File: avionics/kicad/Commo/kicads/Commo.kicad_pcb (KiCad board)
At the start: 4 copper layers, 55 x 35 mm, 81 parts, among them U1 ByA 100nF +3V3 U1-VDDA Bypass, U1 ByB 100nF +3V3 U1-VDD Bypass

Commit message: Migrate fleet TPM from Infineon SLB9670 to SLB9672
Replaces every active reference to the SLB9670 TPM with SLB9672 across
KiCad symbols/schematics/PCBs/netlists, generator scripts, firmware
device-tree overlays, and documentation (REFERENCES.md, WBS/TODO,
current-specification, graphical build guide). Archived files, frozen
revision snapshots, and the old datasheet PDF are left untouched.

- Added avionics/datasheets/SLB_9672XU20_Infineon.pdf (Infineon DS Rev
  1.3, 2024-11-18) and a new clean-room symbol/pinmap
  (Observer_SLB9672_TPM.kicad_sym, SLB9672XU2_0_pinmap.csv), replacing
  the superseded SLB9670 symbol/pinmap.
- Verified the physical footprint is unchanged (5x5mm body, 0.5mm
  pitch, 32-pin QFN, 3.6x3.6mm exposed pad per both datasheets), so the
  existing Package_DFN_QFN:QFN-32-1EP_5x5mm_P0.5mm_EP3.45x3.45mm
  footprint was reused as-is. Pin *functions* do differ (SLB9672 makes
  pins 1/14/22 the mandatory VDD pins vs 8/22 on SLB9670; pin 6 is now a
  true no-connect instead of GPIO; pins 3/4/7 are GPIO_00/01/02 instead
  of NCI/NCI/PP) -- the new symbol and every net-map/pinmap that lists
  pin functions reflect the corrected pinout.
- Populated the corrected component into Observer, Commo, Flight
  Engineer, and CAN-PERIPH-GW-1's schematics (lib_symbol block +
  instances) and into every board's PCB Value/property text. Pilot's
  and XO's own independently-authored inline TPM symbols were text-
  renamed only, preserving their pre-existing (and separately tracked)
  wrong-pin-number defect -- out of scope for this swap.
- Firmware: infineon,slb9670 -> infineon,slb9672 compatible string and
  tpm_slb9670: -> tpm_slb9672: node label in both active cape DTS
  overlays.
- REFERENCES.md REF-SENSOR-011 updated in place with validated Infineon
  URLs; new open items logged for (a) re-running kicad-cli ERC/DRC
  (unavailable in this environment) and (b) a newly-found, unrelated
  pre-existing footprint-mismatch defect on XO's placed TPM.
- PROJECT_INDEX.md / t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
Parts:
- TPM: value SLB9670 -> SLB9672
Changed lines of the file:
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@@
 			)
 		)
-		(property "Value" "SLB9670"
+		(property "Value" "SLB9672"
 			(at 0 -3.83 0)
 			(layer "B.Fab")

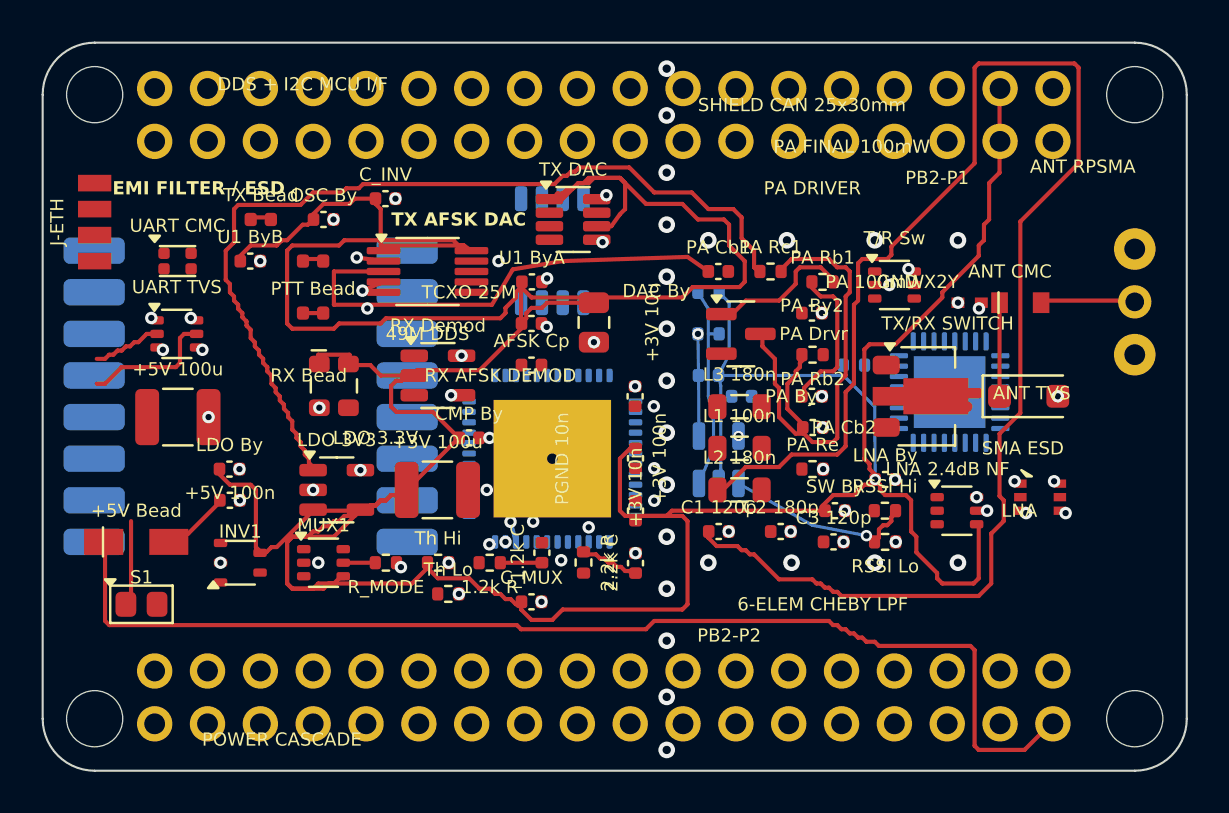
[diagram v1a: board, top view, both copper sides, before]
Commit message: feat(avionics): swap Commo's LoRa (RFM95W) for SiK (RFD900ux-SMT), ERC 0
Completes the other half of the XO<->Commo radio relocation: Commo
gains the SiK link SiK-side via a new one-off script
(swap_lora_for_sik.py) that does direct S-expression surgery rather
than re-running gen_commo_sch.py, which is PCB-first and already
confirmed drifted from the real board. Also fixes two pre-existing
circuit bugs the swap's ERC cleanup exposed: the T/R switch's antenna
pin was on a differently-named net one row away from the working ANT
filter chain (merged); and the PA final transistor's emitter pin was
wired straight to GND, bypassing its own degeneration resistor
(rewired onto PA_EMIT). DDS_FSYNC (the TX DAC's SPI chip-select,
previously unrouted) now uses the exact PB2 pin the LoRa->SiK swap
freed (ex-SPI1_CS_LORA), by explicit owner decision. kicad-cli sch
erc: 0 violations (down from 45).

PCB synced to match (schematic driving PCB, not the reverse): old
RFM95W footprint removed, 8 new SIK-chain footprints added with nets
matched 1:1 against the real schematic pin table. Along the way DRC
caught a real geometry bug in the shared RFDesign_RFD900ux_SMT
footprint (pad pitch/axis swap causing adjacent castellated pins to
short) -- fixed against RFD900ux DataSheet v1.2.pdf Table 6-1 and
confirmed via DRC. Residual: Commo's existing hand-placed layout has
no contiguous free region for the 21x29mm SIK module without touching
ETH-PHY/T-ETH -- flagged in WBS.md as needing a real floorplan pass,
not silently left implicit.

Co-Authored-By: Claude Sonnet 5 <noreply@anthropic.com>
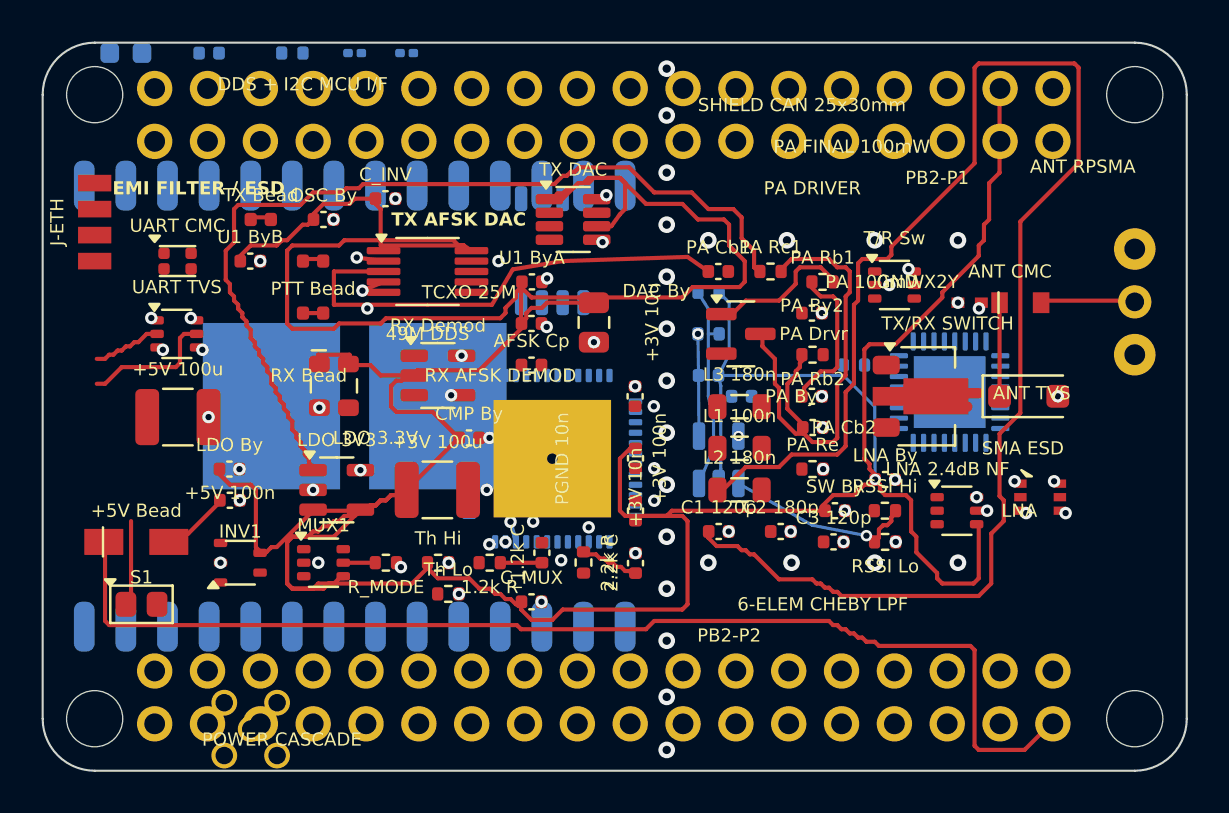
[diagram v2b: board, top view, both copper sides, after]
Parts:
- removed LoRa: RFM95W, HOPERF_RFM9XW_SMD
- added C-SIK-SH1: DNP, C_0201_0603Metric, B.Cu at (115.0, 100.5)
- added C-SIK-SH2: DNP, C_0201_0603Metric, B.Cu at (117.5, 100.5)
- added C-SIK1: 10uF 10V X5R, C_0603_1608Metric, B.Cu at (104.0, 100.5)
- added C-SIK2: 100nF, C_0402_1005Metric, B.Cu at (108.0, 100.5)
- added D-ANT-SIK: RCLAMP0502B, RCLAMP0502B_SOD882, B.Cu at (104.0, 133.0)
- added J-ANT-SIK: MMCX vertical, MMCX_Molex_73415-1471_Vertical, B.Cu at (110.0, 133.0)
- added L-SIK-SER: 0R link, R_0402_1005Metric, B.Cu at (112.0, 100.5)
- added SIK: RFD900ux-SMT, RFDesign_RFD900ux_SMT, B.Cu at (115.0, 117.5)
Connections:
- PA 100mW pad 2: GND -> PA_EMIT
- PB2-P1 pad 10: RS485_RX -> unconnected-(PB2-P1-RS485_RX-Pad10)
- PB2-P1 pad 11: RS485_TX -> unconnected-(PB2-P1-RS485_TX-Pad11)
- PB2-P1 pad 12: CAN_STB -> unconnected-(PB2-P1-CAN_STB-Pad12)
- PB2-P1 pad 13: MCAN1_RX -> unconnected-(PB2-P1-MCAN1_RX-Pad13)
- PB2-P1 pad 14: MCAN1_TX -> unconnected-(PB2-P1-MCAN1_TX-Pad14)
- PB2-P1 pad 19: LORA_RESETN -> SIK_RTS
- PB2-P1 pad 20: LORA_DIO0 -> SIK_CTS
- PB2-P1 pad 22: SPI1_CS_NOR -> unconnected-(PB2-P1-SPI1_CS_NOR-Pad22)
- PB2-P1 pad 26: SPI1_CS_LORA -> DDS_FSYNC
- PB2-P1 pad 27: SDIO_D3 -> unconnected-(PB2-P1-SDIO_D3-Pad27)
- PB2-P1 pad 28: SDIO_D2 -> unconnected-(PB2-P1-SDIO_D2-Pad28)
- PB2-P1 pad 29: SDIO_D1 -> unconnected-(PB2-P1-SDIO_D1-Pad29)
- PB2-P1 pad 3: I2C0_SDA -> unconnected-(PB2-P1-I2C0_SDA-Pad3)
- PB2-P1 pad 30: SDIO_D0 -> unconnected-(PB2-P1-SDIO_D0-Pad30)
- PB2-P1 pad 31: SDIO_CMD -> unconnected-(PB2-P1-SDIO_CMD-Pad31)
- PB2-P1 pad 32: SDIO_CLK -> unconnected-(PB2-P1-SDIO_CLK-Pad32)
- PB2-P1 pad 4: I2C0_SCL -> unconnected-(PB2-P1-I2C0_SCL-Pad4)
- PB2-P1 pad 5: PRU_1553_RX_N -> unconnected-(PB2-P1-PRU_1553_RX_N-Pad5)
- PB2-P1 pad 6: PRU_1553_RX_P -> unconnected-(PB2-P1-PRU_1553_RX_P-Pad6)
- PB2-P1 pad 7: PRU_1553_TX_N -> unconnected-(PB2-P1-PRU_1553_TX_N-Pad7)
- PB2-P1 pad 8: PRU_1553_TX_P -> unconnected-(PB2-P1-PRU_1553_TX_P-Pad8)
- PB2-P1 pad 9: RS485_DE -> unconnected-(PB2-P1-RS485_DE-Pad9)
- PB2-P2 pad 10: WINCH_IN1 -> unconnected-(PB2-P2-WINCH_IN1-Pad10)
- PB2-P2 pad 15: PHY1_RSTN -> unconnected-(PB2-P2-PHY1_RSTN-Pad15)
- PB2-P2 pad 16: PHY1_INTRN -> unconnected-(PB2-P2-PHY1_INTRN-Pad16)
- PB2-P2 pad 27: RMII0_REF_CLK -> unconnected-(PB2-P2-RMII0_REF_CLK-Pad27)
- PB2-P2 pad 28: RMII0_RX_ER -> unconnected-(PB2-P2-RMII0_RX_ER-Pad28)
- PB2-P2 pad 29: RMII0_CRS_DV -> unconnected-(PB2-P2-RMII0_CRS_DV-Pad29)
- PB2-P2 pad 3: PWM_CH3 -> unconnected-(PB2-P2-PWM_CH3-Pad3)
- PB2-P2 pad 30: RMII0_RXD1 -> unconnected-(PB2-P2-RMII0_RXD1-Pad30)
- PB2-P2 pad 31: RMII0_RXD0 -> unconnected-(PB2-P2-RMII0_RXD0-Pad31)
- PB2-P2 pad 32: RMII0_TX_EN -> unconnected-(PB2-P2-RMII0_TX_EN-Pad32)
- PB2-P2 pad 33: RMII0_TXD1 -> unconnected-(PB2-P2-RMII0_TXD1-Pad33)
- PB2-P2 pad 34: RMII0_TXD0 -> unconnected-(PB2-P2-RMII0_TXD0-Pad34)
- PB2-P2 pad 4: PWM_CH2 -> unconnected-(PB2-P2-PWM_CH2-Pad4)
- PB2-P2 pad 5: PWM_CH1 -> unconnected-(PB2-P2-PWM_CH1-Pad5)
- PB2-P2 pad 6: PWM_CH0 -> unconnected-(PB2-P2-PWM_CH0-Pad6)
- PB2-P2 pad 7: LOAD_CELL_DOUT -> unconnected-(PB2-P2-LOAD_CELL_DOUT-Pad7)
- PB2-P2 pad 8: LOAD_CELL_SCK -> unconnected-(PB2-P2-LOAD_CELL_SCK-Pad8)
- PB2-P2 pad 9: WINCH_IN2 -> unconnected-(PB2-P2-WINCH_IN2-Pad9)
- T/R Sw pad 1: RF_ANT_SW -> ANT
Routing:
- net PA_EMIT: track 0.00 -> 5.87 mm
- net GND: track 14.2 -> 8.31 mm, vias 82 -> 81
- net unconnected-(SIK-Pad4): vias 0 -> 1
- net unconnected-(PB2-P1-SPI1_CS_NOR-Pad22): vias 0 -> 1
- net SPI1_CS_NOR: vias 1 -> 0
